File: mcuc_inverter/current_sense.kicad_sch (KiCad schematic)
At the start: 0 parts

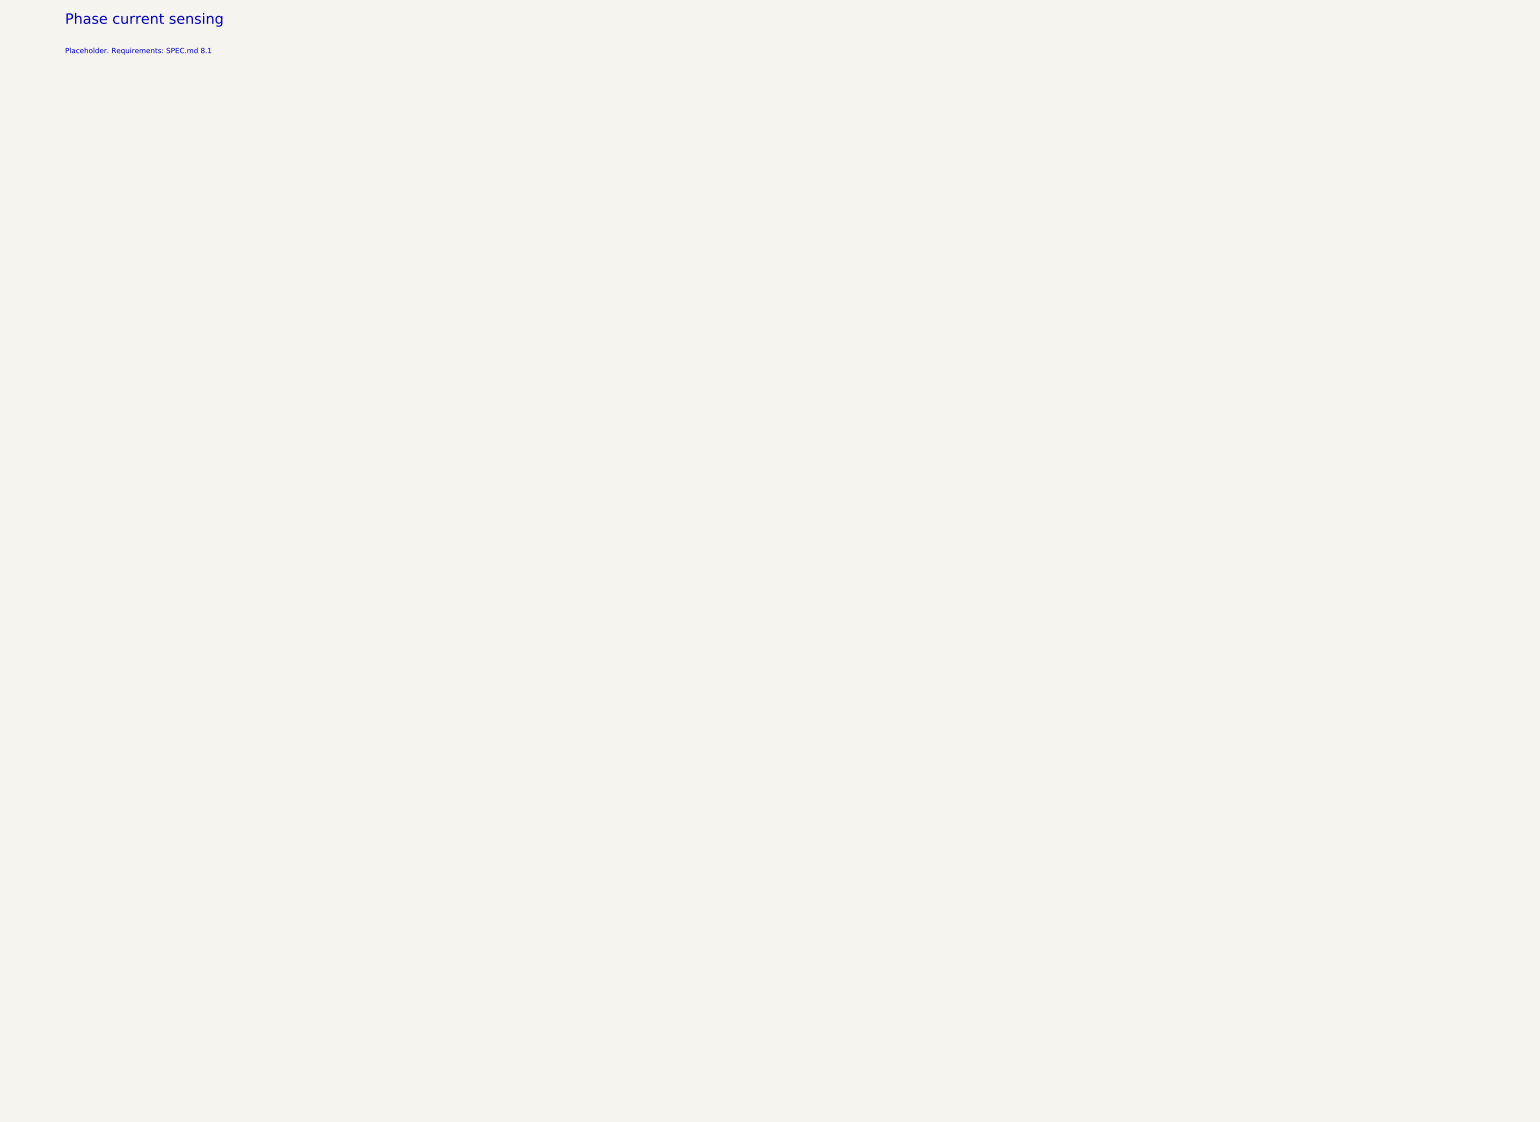
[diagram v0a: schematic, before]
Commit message: Capture current_sense sheet: 3x HOYS 200-S/SP33 + 300 A trip
Per D019: LEM HOYS transducers with explicit primary pins so the
phase busbar path is in the netlist (U201 phase terminal -> P1/P2 ->
PHASE_x_OUT). Pinout verified from the LEM datasheet connection
figure - 5-pin device including an OCD output the brief didn't know
about, wire-OR'd onto OC_TRIP as an independent ~584 A backup trip.

Per phase: 100R/1nF anti-alias to I_PH_x, individual I_REF_x (Uref
outputs may not be paralleled per datasheet), and an LM2903-class
open-drain window comparator pair (thresholds 2.340/0.960 V from a
9.53k/13.7k/9.53k E96 string = +/-300 A at 2.3 mV/A) pulling
OC_TRIP low on either polarity - matching the ported PALTA
active-low wired-OR into R907 + the supervisor edge-maker. No
hysteresis by design: the supervisor latches the first edge; note
on-sheet.

Root: PHASE_U/V/W wired power_stage -> current_sense; OC_TRIP wired
to supervisor. ERC 0 errors; 69/69 netlist checks by the agent;
OC_TRIP membership (exactly 11 nodes) and phase continuity
independently re-verified.

Co-Authored-By: Claude Fable 5 <noreply@anthropic.com>
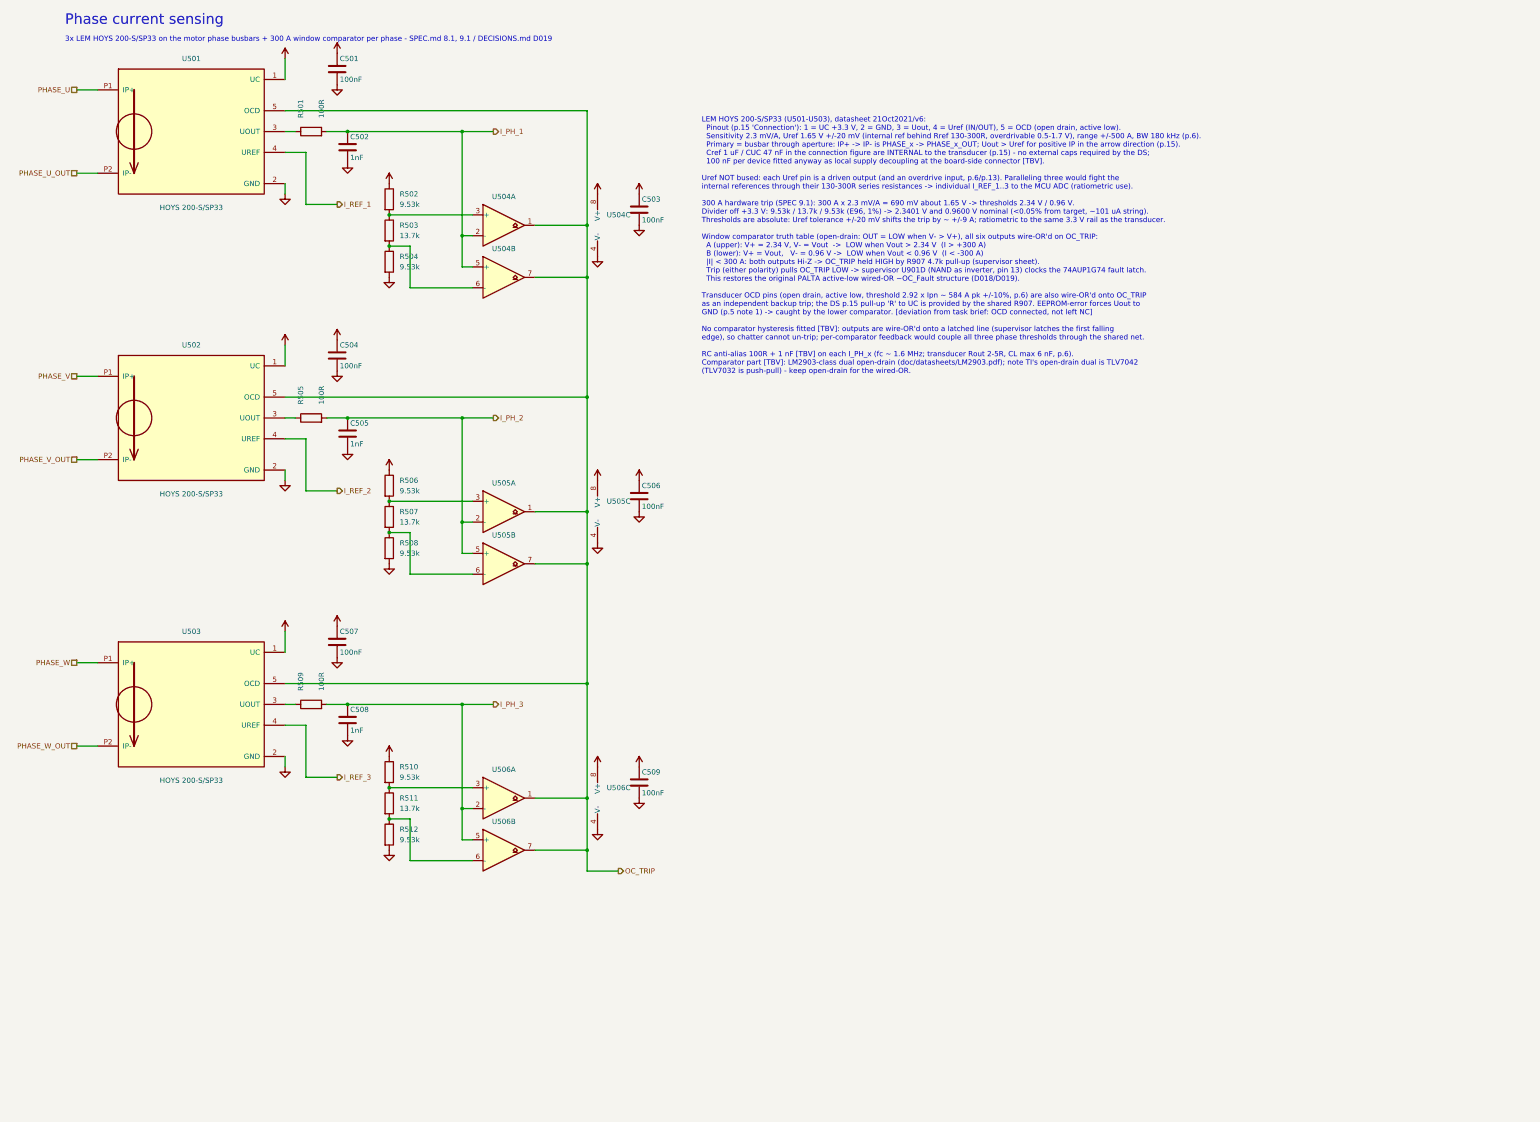
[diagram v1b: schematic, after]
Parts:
- added C501, C503, C504, C506, C507, C509: 100nF, Capacitor_SMD:C_0603_1608Metric, symbol Device:C
- added C502, C505, C508: 1nF, Capacitor_SMD:C_0603_1608Metric, symbol Device:C
- added R501, R505, R509: 100R, Resistor_SMD:R_0603_1608Metric, symbol Device:R
- added R502, R504, R506, R508, R510, R512: 9.53k, Resistor_SMD:R_0603_1608Metric, symbol Device:R
- added R503, R507, R511: 13.7k, Resistor_SMD:R_0603_1608Metric, symbol Device:R
- added U501, U502, U503: HOYS 200-S/SP33, symbol mcuc:HOYS_200-S_SP33
- added U504, U505, U506: TLV7032/LM2903-class open-drain [TBV], Package_SO:SOIC-8_3.9x4.9mm_P1.27mm, symbol Comparator:LM2903
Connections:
- new net: R509.1, U503.3 (UOUT)
- new net: R506.2, R507.1, U505.3 (+)
- new net: R501.1, U501.3 (UOUT)
- new net: R503.2, R504.1, U504.6 (-)
- new net: R502.2, R503.1, U504.3 (+)
- new net: R505.1, U502.3 (UOUT)
- new net: R511.2, R512.1, U506.6 (-)
- new net: R510.2, R511.1, U506.3 (+)
- new net: R507.2, R508.1, U505.6 (-)
- new net +3.3V: C501.1, C503.1, C504.1, C506.1, C507.1, C509.1, R502.1, R506.1, R510.1, U501.1 (UC), U502.1 (UC), U503.1 (UC), U504.8 (V+), U505.8 (V+), U506.8 (V+)
- new net GND: C501.2, C502.2, C503.2, C504.2, C505.2, C506.2, C507.2, C508.2, C509.2, R504.2, R508.2, R512.2, U501.2 (GND), U502.2 (GND), U503.2 (GND), U504.4 (V-), U505.4 (V-), U506.4 (V-)
- new net I_PH_1: C502.1, R501.2, U504.2 (-), U504.5 (+)
- new net I_PH_2: C505.1, R505.2, U505.2 (-), U505.5 (+)
- new net I_PH_3: C508.1, R509.2, U506.2 (-), U506.5 (+)
- new net I_REF_1: U501.4 (UREF)
- new net I_REF_2: U502.4 (UREF)
- new net I_REF_3: U503.4 (UREF)
- new net OC_TRIP: U501.5 (OCD), U502.5 (OCD), U503.5 (OCD), U504.1, U504.7, U505.1, U505.7, U506.1, U506.7
- new net PHASE_U: U501.P1 (IP+)
- new net PHASE_U_OUT: U501.P2 (IP-)
- new net PHASE_V: U502.P1 (IP+)
- new net PHASE_V_OUT: U502.P2 (IP-)
- new net PHASE_W: U503.P1 (IP+)
- new net PHASE_W_OUT: U503.P2 (IP-)
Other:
- note added: "3x LEM HOYS 200-S/SP33 on the motor phase busbars + 300 A window comparator per phase - SPEC.md 8.1, 9.1 / DECISIONS.md D019"
- note added: "LEM HOYS 200-S/SP33 (U501-U503), datasheet 21Oct2021/v6: Pinout (p.15 'Connection'): 1 = UC +3.3 V, 2 = GND, 3 = Uout, 4 = Uref (IN/OUT), 5 = OCD (open drain, active low). Sensitivity 2.3 mV/A, Uref 1.65 V +/-20 mV (internal ref behind Rref 130-300R, overdrivable 0.5-1.7 V), range +/-500 A, BW 180 kHz (p.6). Primary = busbar through aperture: IP+ -> IP- is PHASE_x -> PHASE_x_OUT; Uout > Uref for 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"
- note removed: "Placeholder. Requirements: SPEC.md 8.1"

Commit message: Board-prep: footprint audit complete, HV terminals, off-board flags
474-component audit: 466 valid resolved footprints, 13 off-board
exclusions per D024 (caps to carrier, chassis resistors, HOYS), 4
flagged TBDs (custom flyback + 3 unchosen inductors), zero silent
gaps. Netlist-fatal fixes: Q403 renumbered to Wolfspeed TO-263-7
convention (G1/KS2/S3-7/tab-D8), CSD18543Q3A remapped to KiCad's
SSSGD VSON-8 pairing - both verified in the netlist afterward.

New HV interface terminals J401-J405 (M4 ring-lug pads: DC input,
precharge-R chassis loop, discharge-R return, bus taps) and HOYS
harness headers J501-J503 (JST 2mm; PA-vs-PH footprint flagged TBV)
with net membership machine-verified incl. the OC_TRIP wire-OR and
I_REF paths to the MCU ADCs.

ERC 0 errors, warnings 201 -> 200 (none introduced).

Co-Authored-By: Claude Fable 5 <noreply@anthropic.com>
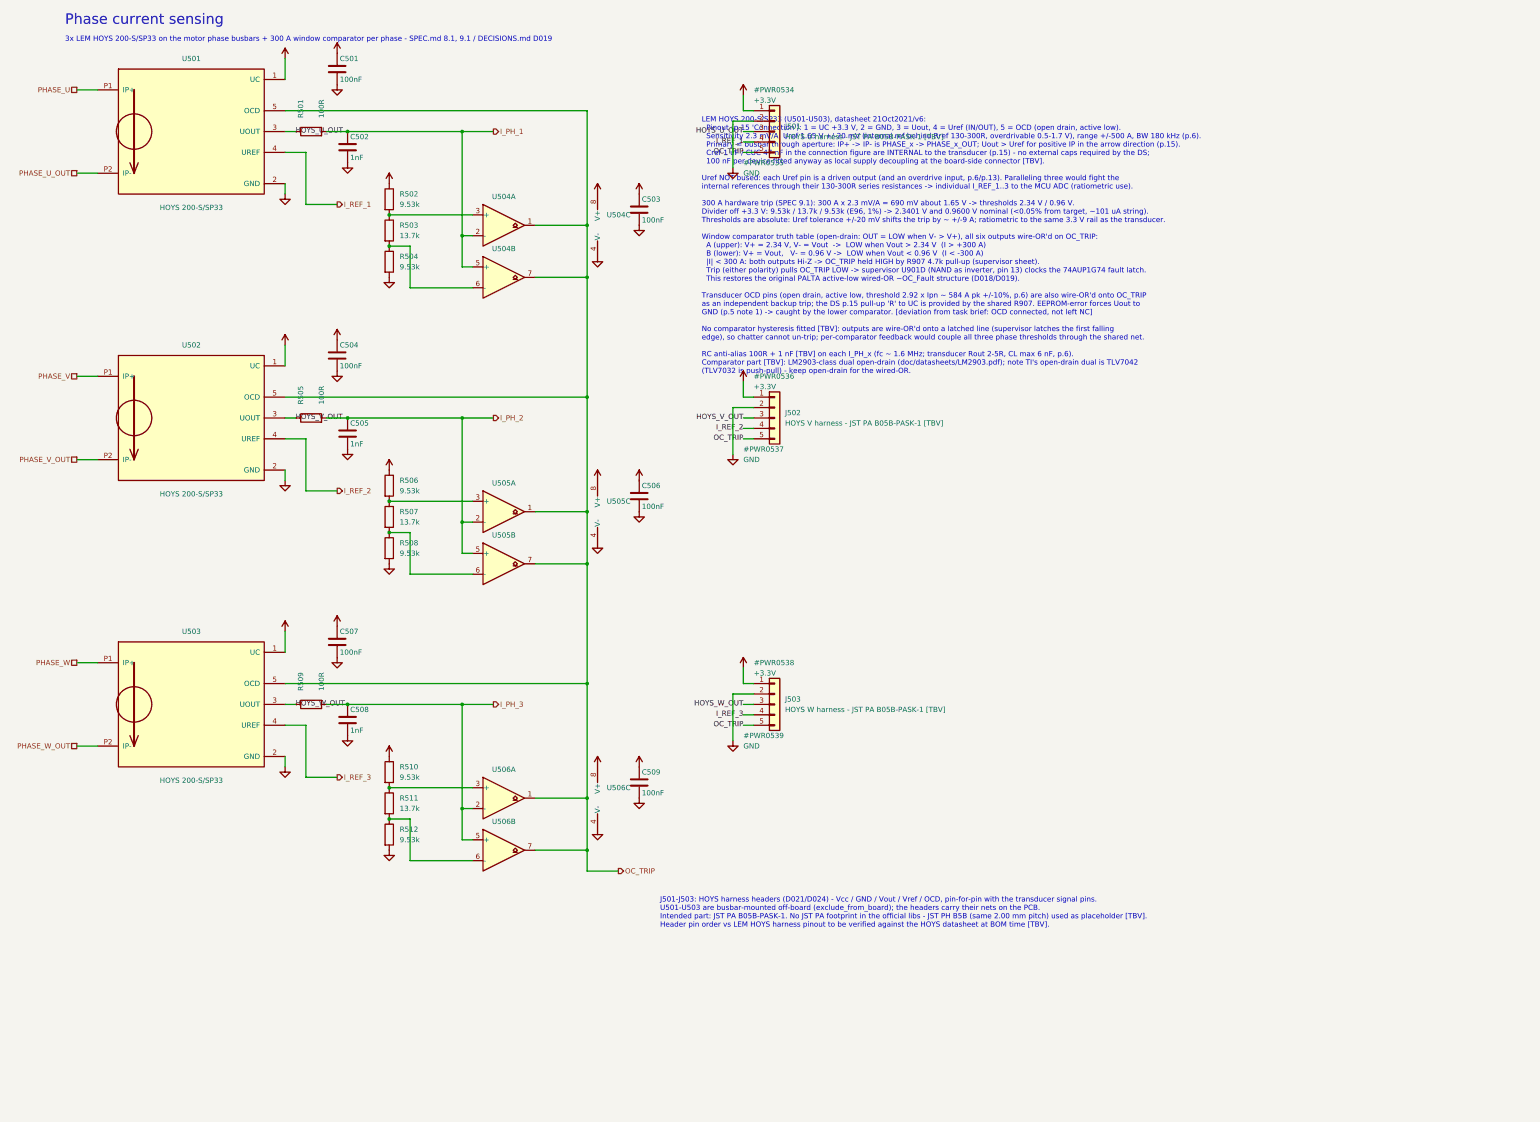
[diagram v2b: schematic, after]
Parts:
- added J501: HOYS U harness - JST PA B05B-PASK-1 [TBV], Connector_JST:JST_PH_B5B-PH-K_1x05_P2.00mm_Vertical, symbol Connector_Generic:Conn_01x05
- added J502: HOYS V harness - JST PA B05B-PASK-1 [TBV], Connector_JST:JST_PH_B5B-PH-K_1x05_P2.00mm_Vertical, symbol Connector_Generic:Conn_01x05
- added J503: HOYS W harness - JST PA B05B-PASK-1 [TBV], Connector_JST:JST_PH_B5B-PH-K_1x05_P2.00mm_Vertical, symbol Connector_Generic:Conn_01x05
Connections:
- net +3.3V: now also J501.1 (Pin_1), J502.1 (Pin_1), J503.1 (Pin_1)
- net GND: now also J501.2 (Pin_2), J502.2 (Pin_2), J503.2 (Pin_2)
- net I_REF_1: now also J501.4 (Pin_4)
- net I_REF_2: now also J502.4 (Pin_4)
- net I_REF_3: now also J503.4 (Pin_4)
- net OC_TRIP: now also J501.5 (Pin_5), J502.5 (Pin_5), J503.5 (Pin_5)
- net HOYS_W_OUT: now reaches R509.1, U503.3 (UOUT)
- net HOYS_W_OUT: now also J503.3 (Pin_3)
- net HOYS_U_OUT: now reaches R501.1, U501.3 (UOUT)
- net HOYS_U_OUT: now also J501.3 (Pin_3)
- net HOYS_V_OUT: now reaches R505.1, U502.3 (UOUT)
- net HOYS_V_OUT: now also J502.3 (Pin_3)
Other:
- note added: "J501-J503: HOYS harness headers (D021/D024) - Vcc / GND / Vout / Vref / OCD, pin-for-pin with the transducer signal pins. U501-U503 are busbar-mounted off-board (exclude_from_board); the headers carry their nets on the PCB. Intended part: JST PA B05B-PASK-1. No JST PA footprint in the official libs - JST PH B5B (same 2.00 mm pitch) used as placeholder [TBV]. Header pin order vs LEM HOYS harness p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"
